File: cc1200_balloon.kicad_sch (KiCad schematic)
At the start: 0 parts

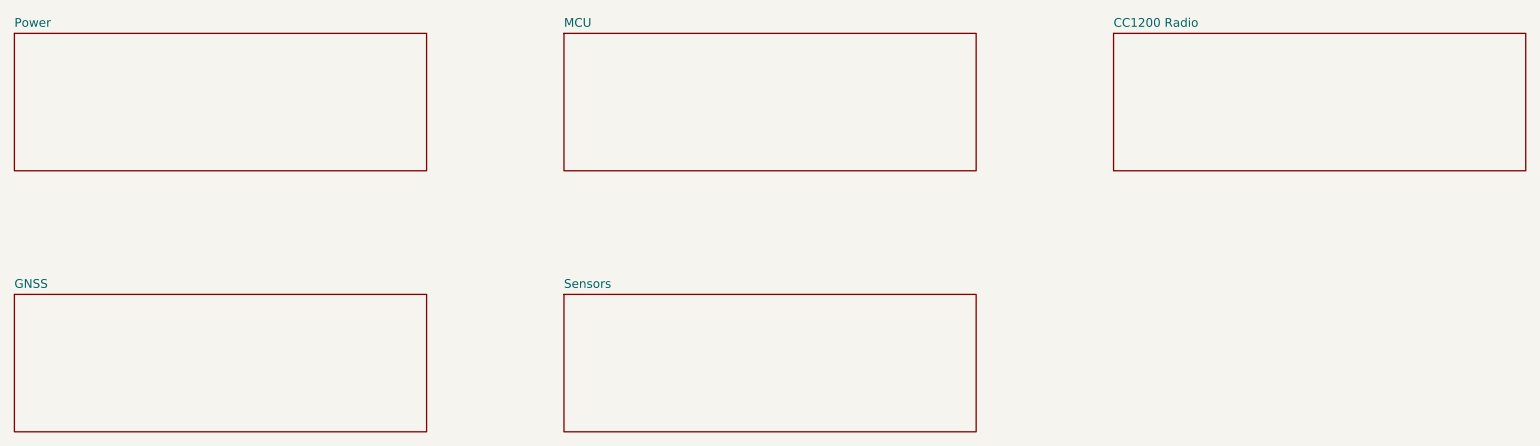
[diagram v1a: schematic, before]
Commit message: Fix DRC errors.
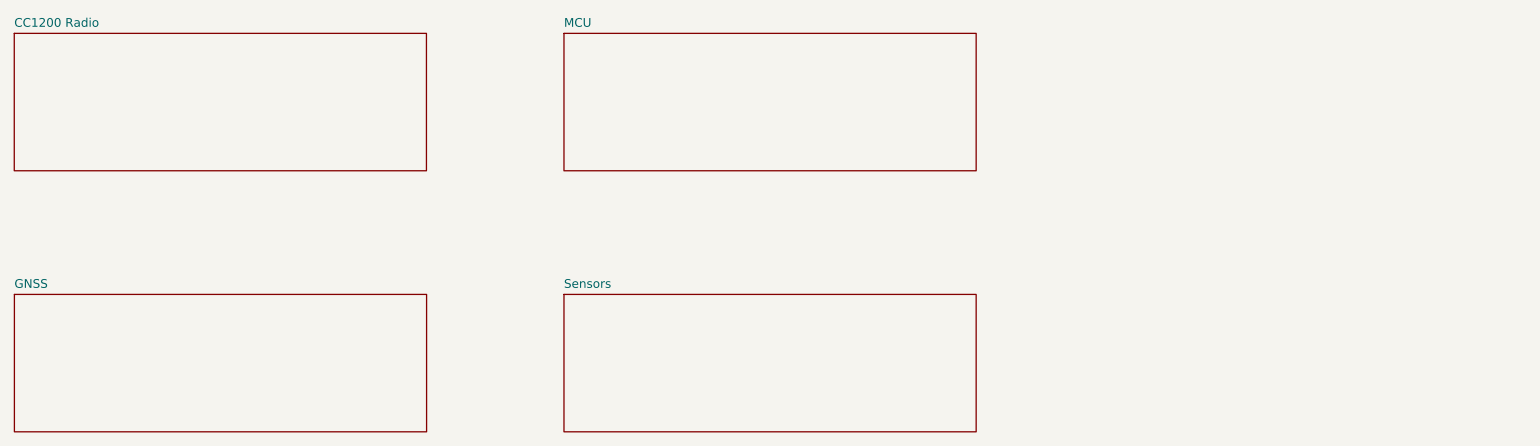
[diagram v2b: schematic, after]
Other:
- removed sheet Power
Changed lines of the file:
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@@
 	)
 	(sheet
-		(at 190 40)
+		(at 29.98 40)
 		(size 60 20)
 		(exclude_from_sim no)
@@
 		)
 		(property "Sheetname" "CC1200 Radio"
-			(at 190 39.2 0)
+			(at 29.98 39.2 0)
 			(show_name no)
 			(do_not_autoplace no)
@@
 		)
 		(property "Sheetfile" "radio.kicad_sch"
-			(at 190 60.8 0)
+			(at 29.98 60.8 0)
 			(hide yes)
 			(show_name no)
@@
 				)
 			)
-		)
-	)
-	(sheet
-		(at 30 40)
-		(size 60 20)
-		(exclude_from_sim no)
-		(in_bom yes)
-		(on_board yes)
-		(dnp no)
-		(fields_autoplaced yes)
-		(stroke
-			(width 0.1524)
-			(type solid)
-		)
-		(fill
-			(color 0 0 0 0)
-		)
-		(property "Sheetname" "Power"
-			(at 30 39.2 0)
-			(show_name no)
-			(do_not_autoplace no)
-			(effects
-				(font
-					(size 1.27 1.27)
-				)
-				(justify left bottom)
-			)
-		)
-		(property "Sheetfile" "power.kicad_sch"
-			(at 30 60.8 0)
-			(hide yes)
-			(show_name no)
-			(do_not_autoplace no)
-			(effects
-				(font
-					(size 1.27 1.27)
-				)
-				(justify left top)
-			)
-		)
-		(instances
-			(project "cc1200_balloon"
-				(path "/5283d11e-ccf0-51c0-83df-1e782a317298"
-					(page "2")
-				)
-			)
